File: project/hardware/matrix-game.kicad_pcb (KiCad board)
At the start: 2 copper layers, 100 x 100 mm, 32 parts, among them SW1 button_center, SW2 button_left, SW3 button_down, SW4 button_right, SW5 button_up, U1 NUCLEO-F042K6, U2 MAX7219, U3 SSD1306

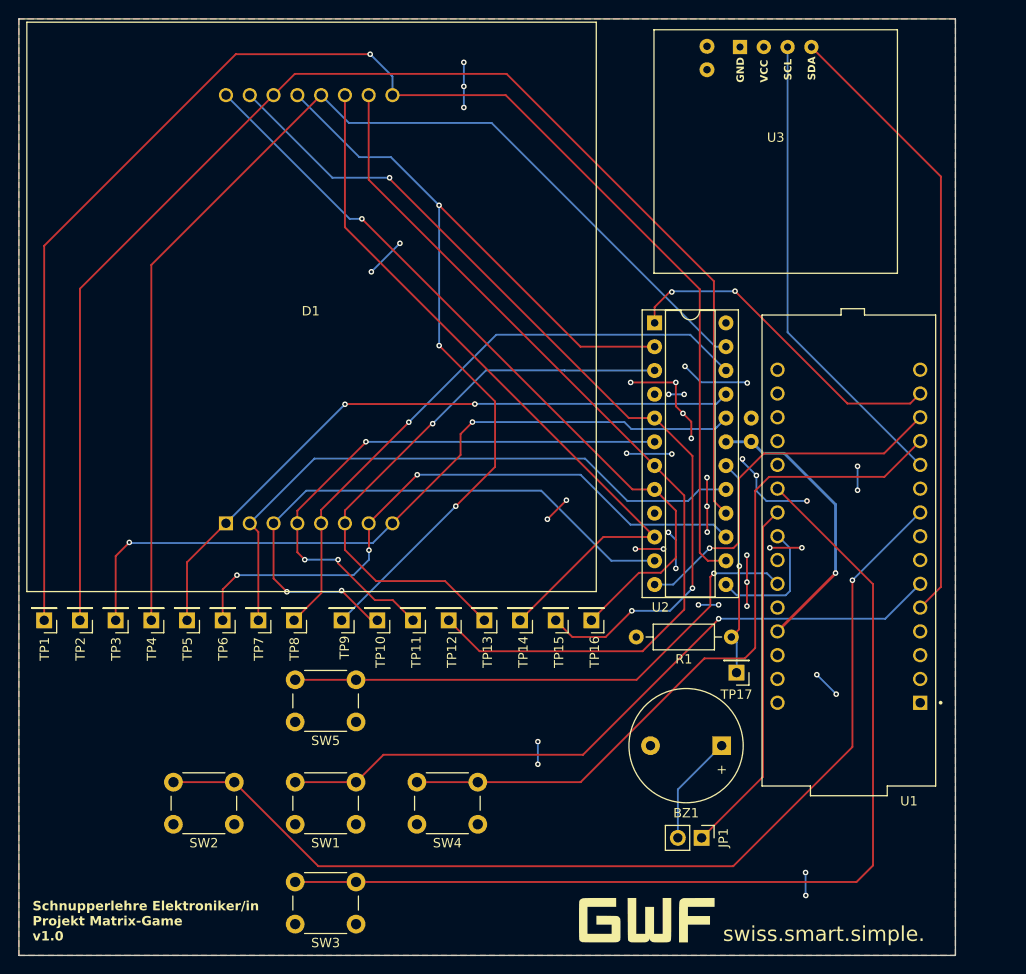
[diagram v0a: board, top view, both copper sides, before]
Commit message: [project/hardware] added library model for LCD, added sockets for Nucleo and LCD
Signed-off-by: Timon Burkard <timon.burkard@gwf.ch>
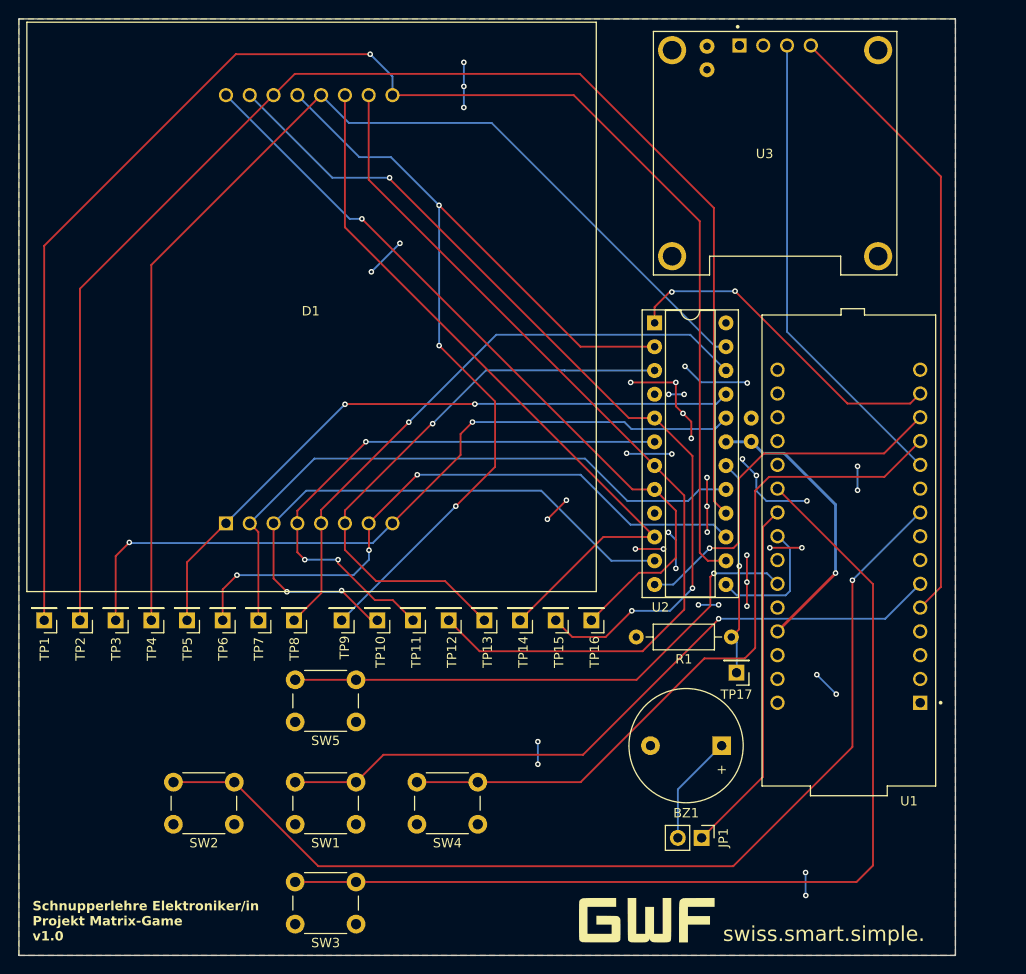
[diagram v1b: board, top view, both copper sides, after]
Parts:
- U3: value SSD1306 -> DM-OLED096-636; footprint Custom_Library:LCD_I2C -> DM-OLED096-636:MODULE_DM-OLED096-636
- moved U3 1.18 mm to (170.8, 59.3)
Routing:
- net Net-(D1-R2): track 147.1 -> 151.7 mm
- net Net-(D1-R1): track 161.3 -> 165.6 mm
